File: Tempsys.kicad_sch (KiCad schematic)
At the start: 15 parts, among them J1 6P4C, J2 prog, J3 gpio, SW1 Reset, U1 E73-2G4M08S1CX, Y1 Crystal

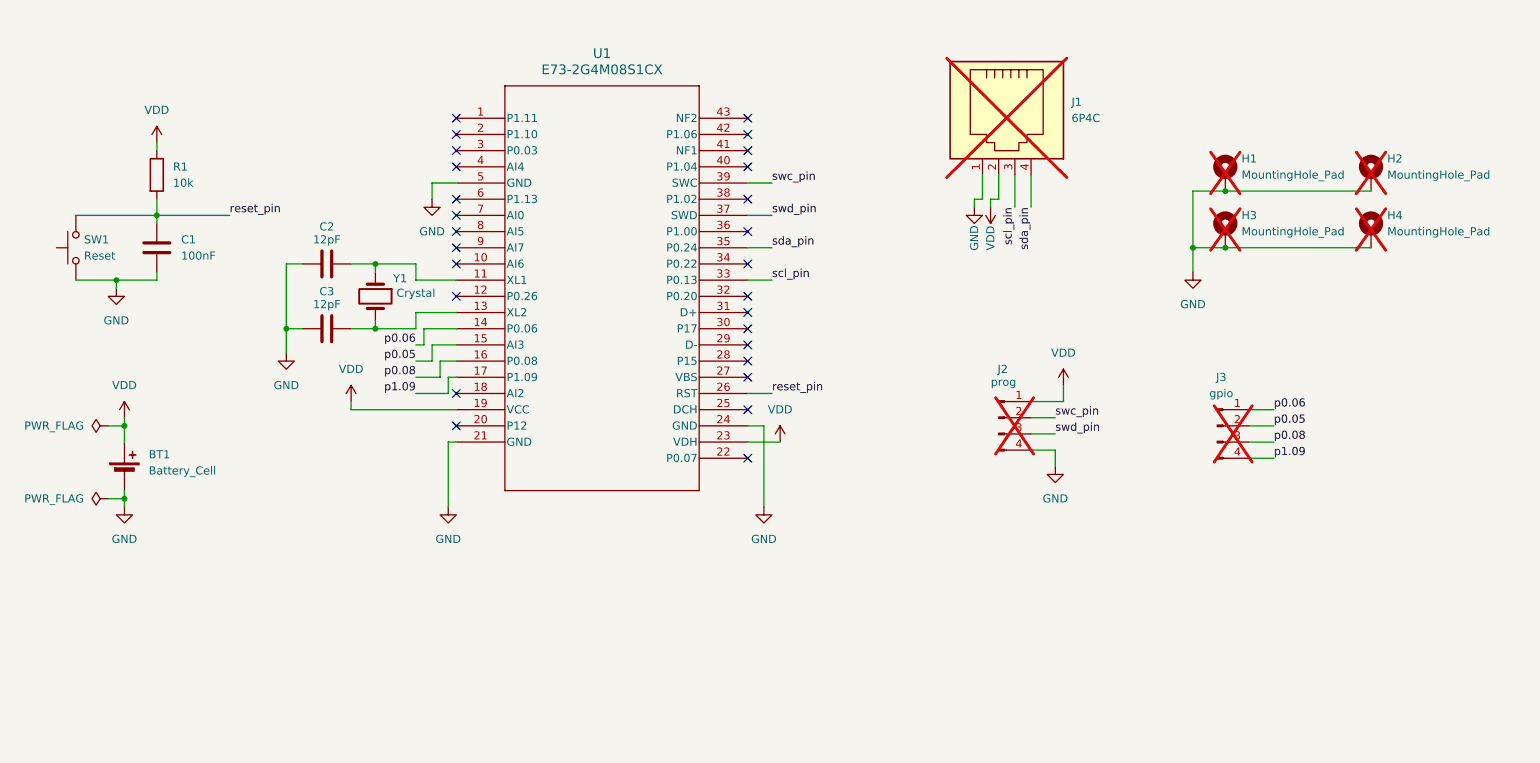
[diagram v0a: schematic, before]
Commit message: Adding pull-ups and jumpers. Also fixing the RJ11 footprint
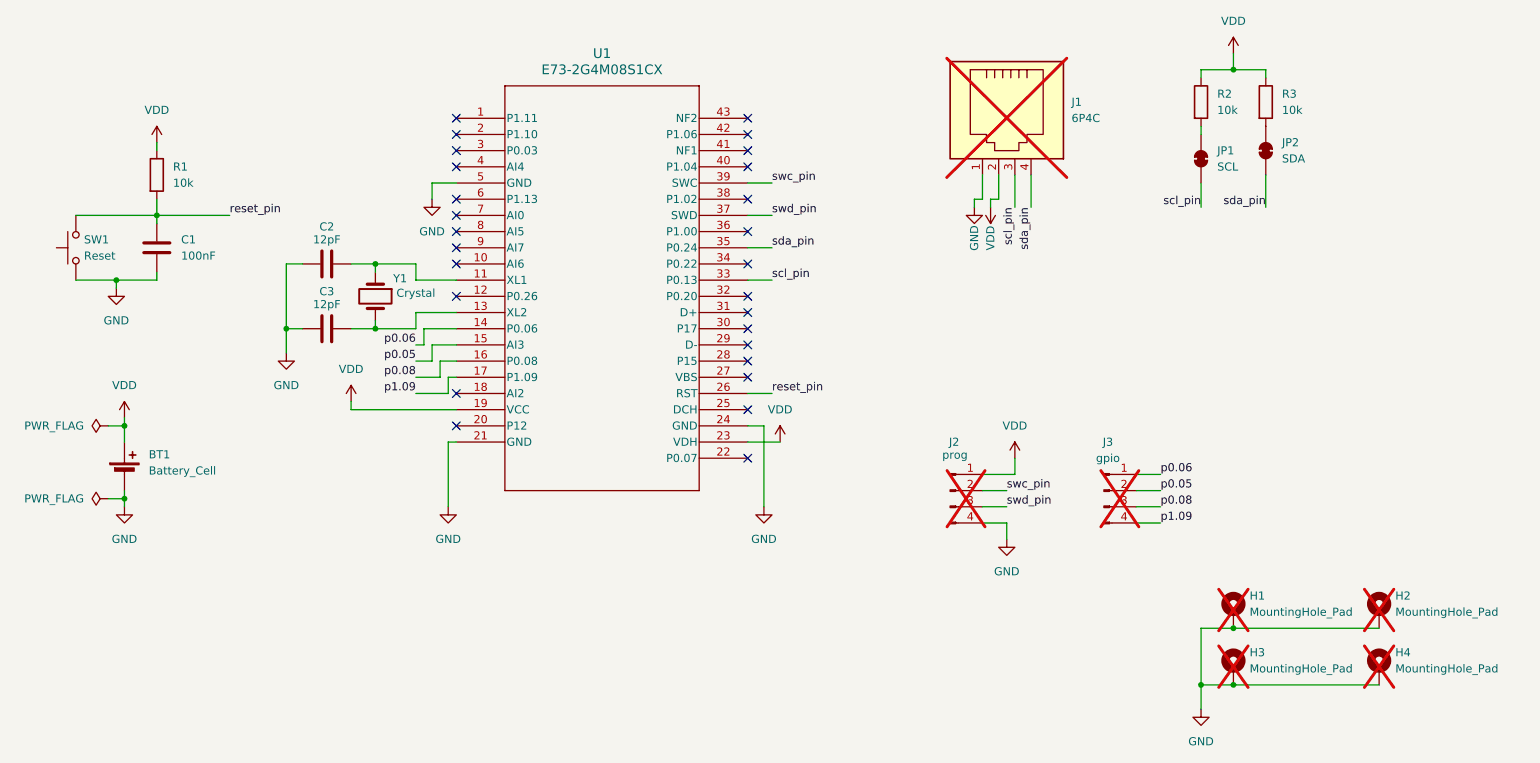
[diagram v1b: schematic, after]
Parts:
- added JP1: SCL, Jumper:SolderJumper-2_P1.3mm_Bridged_RoundedPad1.0x1.5mm, symbol Jumper:SolderJumper_2_Bridged
- added JP2: SDA, Jumper:SolderJumper-2_P1.3mm_Bridged_RoundedPad1.0x1.5mm, symbol Jumper:SolderJumper_2_Bridged
- added R2, R3: 10k, Resistor_SMD:R_0402_1005Metric, symbol Device:R
- J1: footprint Connector_RJ:RJ14_Connfly_DS1133-S4_Horizontal -> Tempsys:438600003
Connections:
- net VDD: now also R2.1, R3.1
- net scl_pin: now also JP1.1 (A)
- net sda_pin: now also JP2.1 (A)
- new net: JP1.2 (B), R2.2
- new net: JP2.2 (B), R3.2
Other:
- moved on the sheet: H1, H2, H3, H4, J2, J3
